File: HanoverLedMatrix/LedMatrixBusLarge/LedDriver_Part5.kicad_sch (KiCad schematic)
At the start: 150 parts

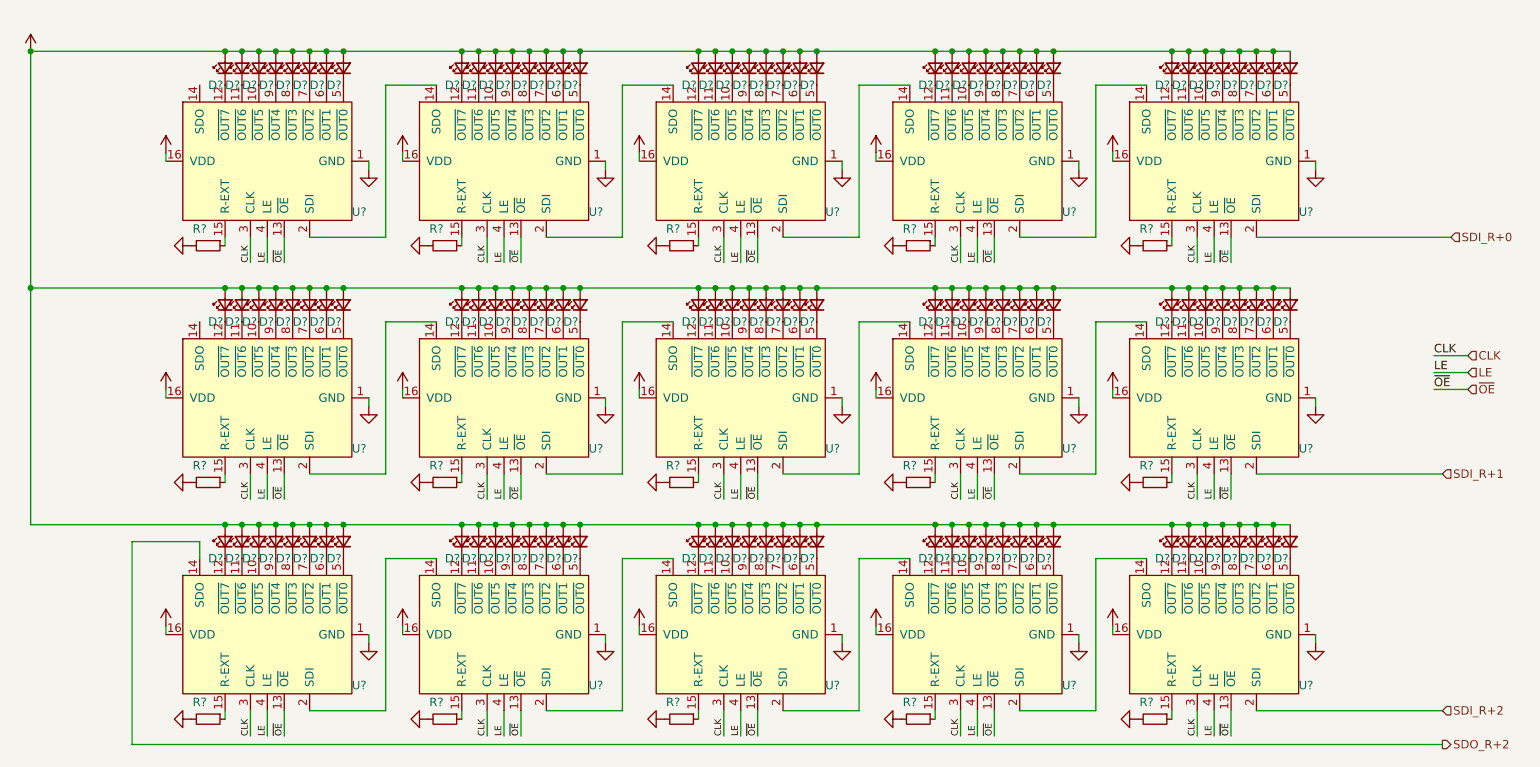
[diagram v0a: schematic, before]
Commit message: feat: Updated the symbol of 74HC373D
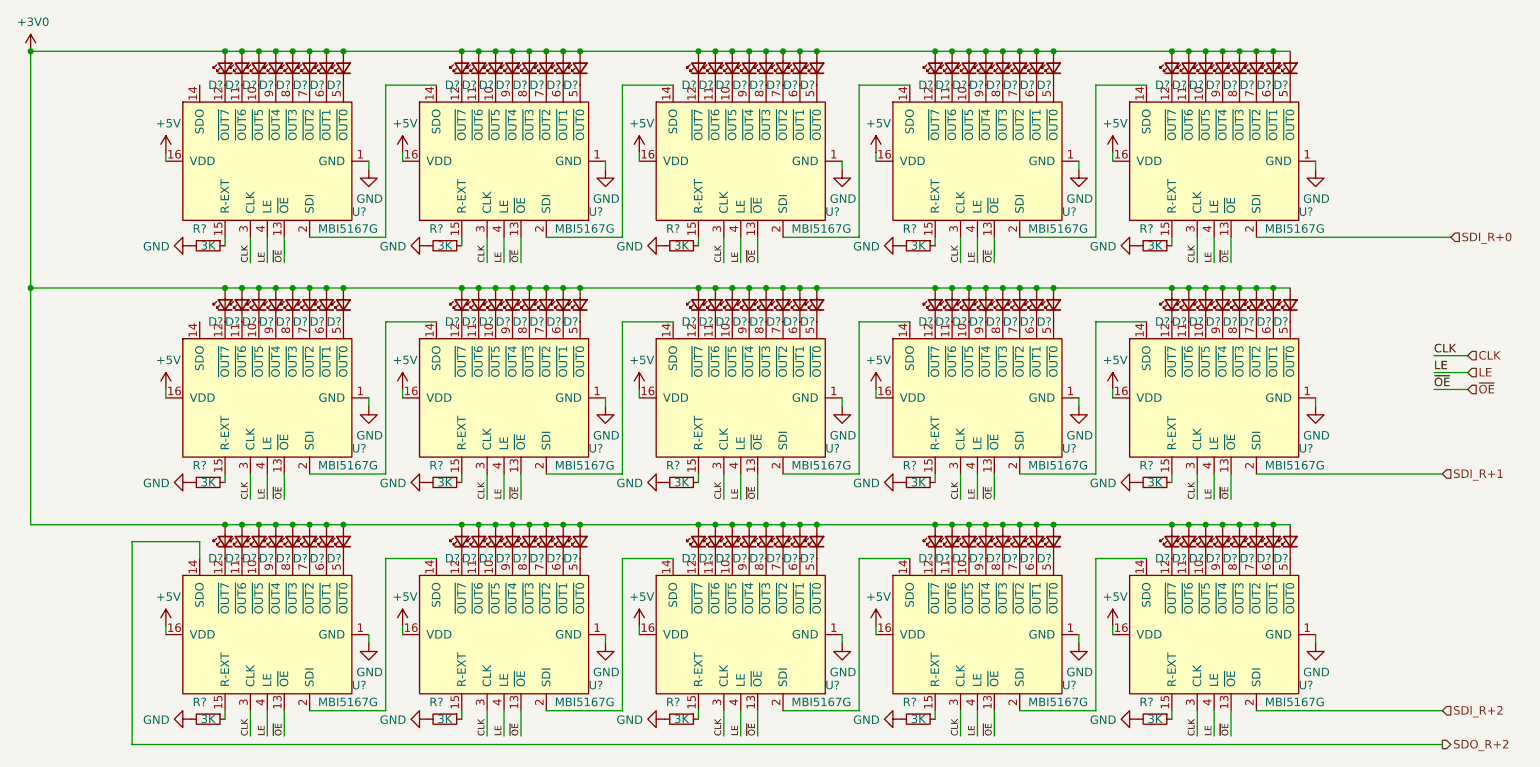
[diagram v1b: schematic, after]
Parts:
- D? (x120): value (none) -> LED_Small
- R? (x15): value (none) -> 3K
- U? (x15): value (none) -> MBI5167G

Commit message: feat: organised the schematic into blocks and updated the readme
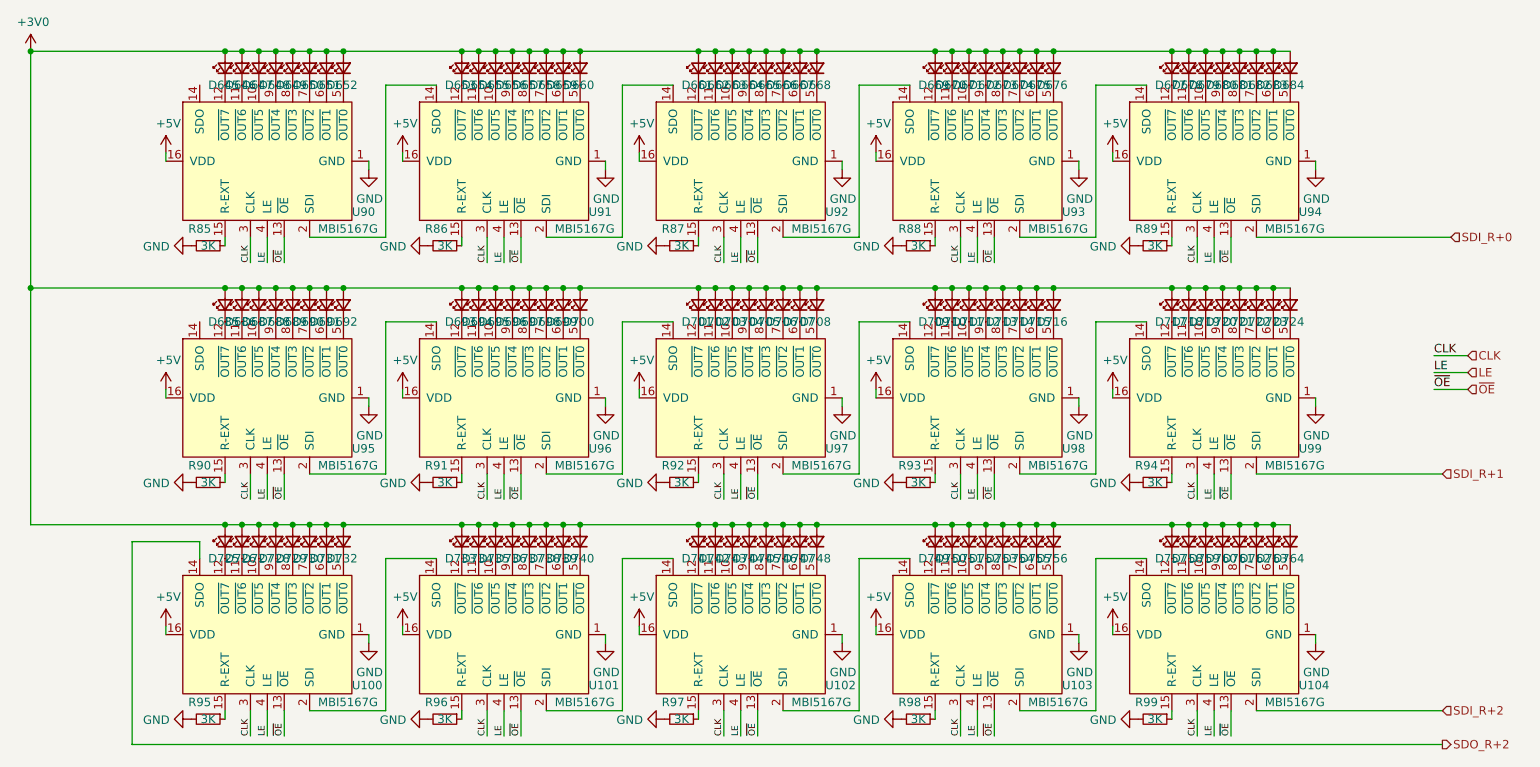
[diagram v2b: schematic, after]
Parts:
- gave numbers to parts that had none: 150
